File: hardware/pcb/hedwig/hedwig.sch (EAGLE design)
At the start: 98 parts, among them J1 PUSHBUTTON, J2 USB4110-GF-A, J3 SMA_EDGE, P1 JTAG-10MINI, Q2 IRLML6402, Q3 20V/0.2A/8MHz/1.2Ω/1Vth, Q6 20V/0.2A/8MHz/1.2Ω/1Vth, U1 NRF24L01SMD, U10 2450LP14A100T, U2 TEXAS_INSTRUMENTS_TLC59731DRT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, U3 FT232RQ, U4 TPS7A26-1.8, U5 ADP2302, U6 RFX2401C, U7 MPL3115A2LGA, U8 STM32F412RE-S, U9 ICM-20948, X1 8M, X2 32.768, X3 ABM8-16.000MHZ-B2-T

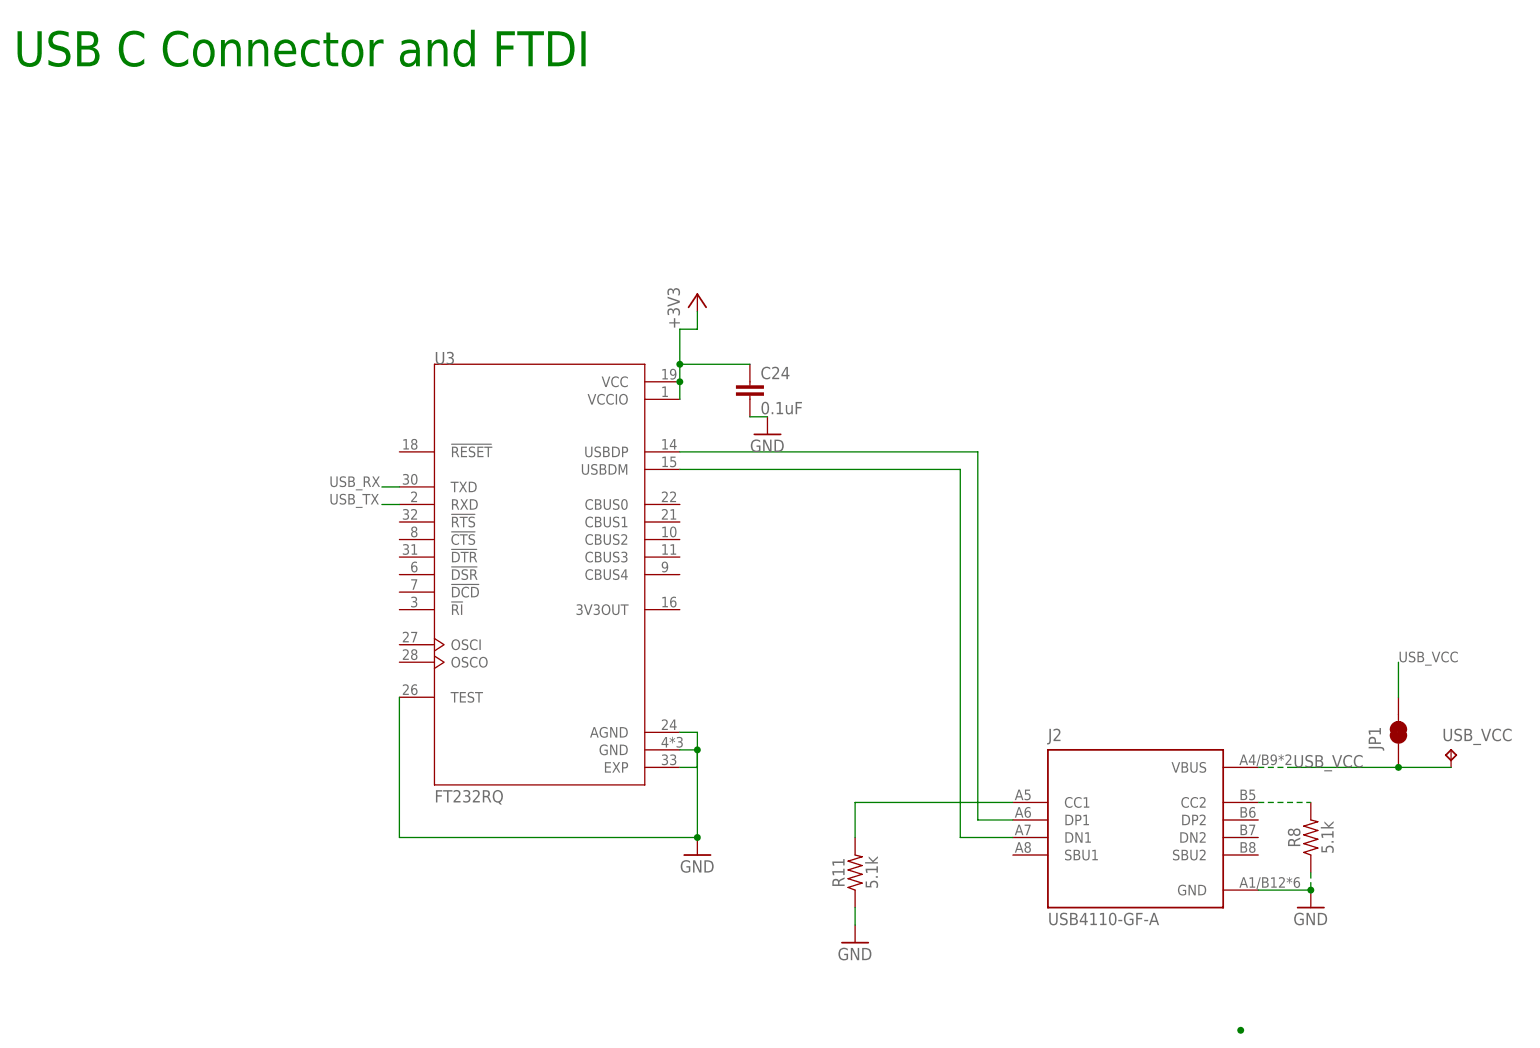
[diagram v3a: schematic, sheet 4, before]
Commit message: Schematic Update  - Fix USB C port reversablilty issue Board Update  - Fix USB C port reversablilty issue BOM Update  - Fix incorrect logic level shift FET  - Fix multiple entries for same parts
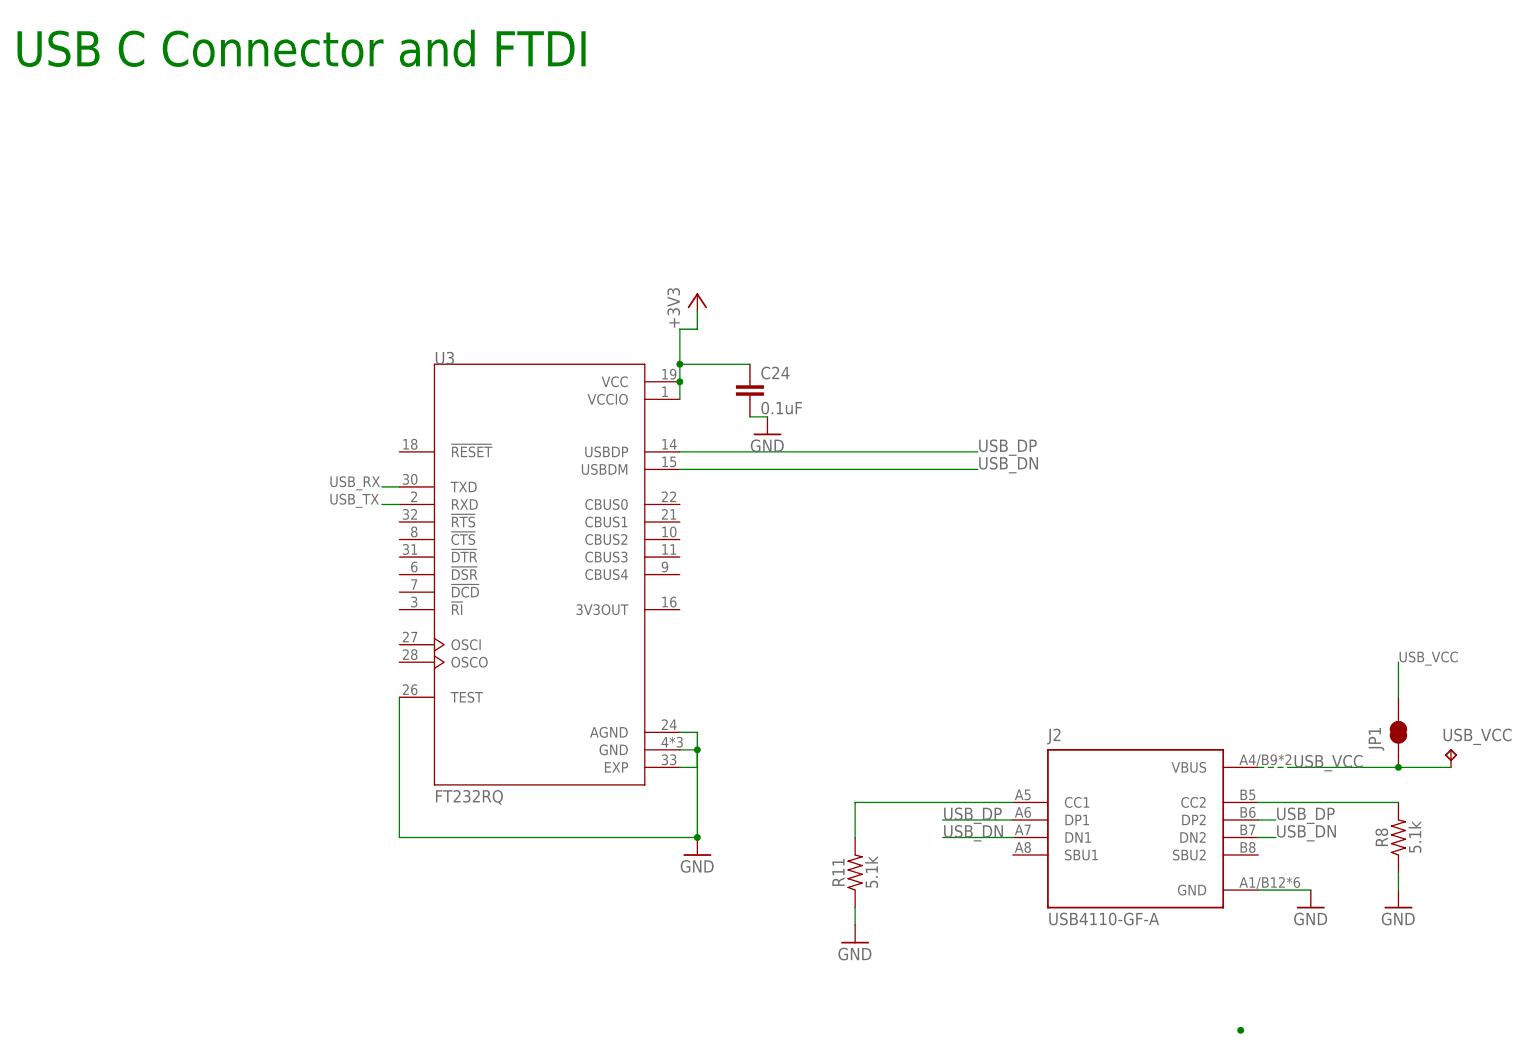
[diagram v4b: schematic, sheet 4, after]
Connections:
- removed net N$21: J2.DP1, U3.USBDP
- removed net N$22: J2.DN1, U3.USBDM
- new net USB_DN: J2.DN1, J2.DN2, U3.USBDM
- new net USB_DP: J2.DP1, J2.DP2, U3.USBDP
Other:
- moved on the sheet: R8
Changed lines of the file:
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@@
 <part name="GND42" library="SparkFun-Aesthetics" deviceset="GND" device=""/>
 <part name="L4" library="falcon" deviceset="REG_INDUCTOR" device="" value="3uH"/>
+<part name="GND43" library="supply1" library_urn="urn:adsk.eagle:library:371" deviceset="GND" device=""/>
 </parts>
 <sheets>
@@
 <attribute name="VALUE" x="83.82" y="-15.24" size="1.778" layer="96" font="vector" rot="R90" align="top-left"/>
 </instance>
-<instance part="R8" gate="R1" x="68.58" y="-27.94" smashed="yes" rot="R90">
-<attribute name="NAME" x="67.056" y="-27.94" size="1.778" layer="95" font="vector" rot="R90" align="bottom-center"/>
-<attribute name="VALUE" x="70.104" y="-27.94" size="1.778" layer="96" font="vector" rot="R90" align="top-center"/>
+<instance part="R8" gate="R1" x="81.28" y="-27.94" smashed="yes" rot="R90">
+<attribute name="NAME" x="79.756" y="-27.94" size="1.778" layer="95" font="vector" rot="R90" align="bottom-center"/>
+<attribute name="VALUE" x="82.804" y="-27.94" size="1.778" layer="96" font="vector" rot="R90" align="top-center"/>
 </instance>
 <instance part="R11" gate="R1" x="2.54" y="-33.02" smashed="yes" rot="R90">
@@
 <attribute name="NAME" x="30.48" y="-13.97" size="1.778" layer="95"/>
 <attribute name="VALUE" x="30.48" y="-40.64" size="1.778" layer="96"/>
+</instance>
+<instance part="GND43" gate="1" x="81.28" y="-38.1" smashed="yes">
+<attribute name="VALUE" x="78.74" y="-40.64" size="1.778" layer="96"/>
 </instance>
 </instances>
@@
 </busses>
 <nets>
-<net name="N$21" class="0">
+<net name="USB_DP" class="0">
 <segment>
 <pinref part="U3" gate="G$1" pin="USBDP"/>
 <wire x1="-22.86" y1="27.94" x2="20.32" y2="27.94" width="0.1524" layer="91"/>
+<label x="20.32" y="27.94" size="1.778" layer="95"/>
+</segment>
+<segment>
 <pinref part="J2" gate="G$1" pin="DP1"/>
-<wire x1="25.4" y1="-25.4" x2="20.32" y2="-25.4" width="0.1524" layer="91"/>
-<wire x1="20.32" y1="-25.4" x2="20.32" y2="27.94" width="0.1524" layer="91"/>
-</segment>
-</net>
-<net name="N$22" class="0">
+<label x="15.24" y="-25.4" size="1.778" layer="95"/>
+<wire x1="25.4" y1="-25.4" x2="15.24" y2="-25.4" width="0.1524" layer="91"/>
+</segment>
+<segment>
+<pinref part="J2" gate="G$1" pin="DP2"/>
+<wire x1="60.96" y1="-25.4" x2="63.5" y2="-25.4" width="0.1524" layer="91"/>
+<label x="63.5" y="-25.4" size="1.778" layer="95"/>
+</segment>
+</net>
+<net name="USB_DN" class="0">
 <segment>
 <pinref part="U3" gate="G$1" pin="USBDM"/>
-<wire x1="-22.86" y1="25.4" x2="17.78" y2="25.4" width="0.1524" layer="91"/>
+<wire x1="-22.86" y1="25.4" x2="20.32" y2="25.4" width="0.1524" layer="91"/>
+<label x="20.32" y="25.4" size="1.778" layer="95"/>
+</segment>
+<segment>
 <pinref part="J2" gate="G$1" pin="DN1"/>
-<wire x1="25.4" y1="-27.94" x2="17.78" y2="-27.94" width="0.1524" layer="91"/>
-<wire x1="17.78" y1="-27.94" x2="17.78" y2="25.4" width="0.1524" layer="91"/>
+<wire x1="25.4" y1="-27.94" x2="15.24" y2="-27.94" width="0.1524" layer="91"/>
+<label x="15.24" y="-27.94" size="1.778" layer="95"/>
+</segment>
+<segment>
+<pinref part="J2" gate="G$1" pin="DN2"/>
+<wire x1="60.96" y1="-27.94" x2="63.5" y2="-27.94" width="0.1524" layer="91"/>
+<label x="63.5" y="-27.94" size="1.778" layer="95"/>
 </segment>
 </net>
@@
 <pinref part="GND20" gate="1" pin="GND"/>
 <wire x1="68.58" y1="-35.56" x2="60.96" y2="-35.56" width="0.1524" layer="91"/>
+</segment>
+<segment>
 <pinref part="R8" gate="R1" pin="1"/>
-<wire x1="68.58" y1="-33.02" x2="68.58" y2="-35.56" width="0.1524" layer="91" style="longdash"/>
-<junction x="68.58" y="-35.56"/>
+<pinref part="GND43" gate="1" pin="GND"/>
+<wire x1="81.28" y1="-35.56" x2="81.28" y2="-33.02" width="0.1524" layer="91"/>
 </segment>
 </net>
@@
 </segment>
 </net>
-<net name="N$15" class="0">
+<net name="N$7" class="0">
 <segment>
 <pinref part="J2" gate="G$1" pin="CC2"/>
 <pinref part="R8" gate="R1" pin="2"/>
-<wire x1="60.96" y1="-22.86" x2="68.58" y2="-22.86" width="0.1524" layer="91" style="longdash"/>
-</segment>
-</net>
+<wire x1="60.96" y1="-22.86" x2="81.28" y2="-22.86" width="0.1524" layer="91"/>
+</segment>
+</net>
